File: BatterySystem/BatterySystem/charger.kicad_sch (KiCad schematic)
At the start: 0 parts

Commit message: BQ25895 toegevoegd in test pcb
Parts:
- added U2: BQ25895RTW, Package_DFN_QFN:Texas_S-PWQFN-N24_EP2.7x2.7mm_ThermalVias, symbol Battery_Management:BQ25895RTW
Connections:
- new net: U2.13 (BAT), U2.14 (BAT)
- new net: U2.15 (SYS), U2.16 (SYS)
- new net: U2.17 (PGND), U2.18 (PGND), U2.25 (PGND)
- new net: U2.19 (SW), U2.20 (SW)
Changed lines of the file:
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@@
 (kicad_sch (version 20230121) (generator eeschema)
   (paper "A4")
+  (symbol (lib_id "Battery_Management:BQ25895RTW") (at 119.38 93.98 0) (unit 1)
+    (in_bom yes) (on_board yes) (dnp no) (fields_autoplaced)
+    (property "Reference" "U2" (at 119.38 70.6501 0)
+      (effects (font (size 1.27 1.27)))
+    )
+    (property "Value" "BQ25895RTW" (at 119.38 72.5711 0)
+      (effects (font (size 1.27 1.27)))
+    )
+    (property "Footprint" "Package_DFN_QFN:Texas_S-PWQFN-N24_EP2.7x2.7mm_ThermalVias" (at 116.84 68.58 0)
+      (effects (font (size 1.27 1.27)) hide)
+    )
+    (property "Datasheet" "http://www.ti.com/lit/ds/symlink/bq25895.pdf" (at 114.3 73.66 0)
+      (effects (font (size 1.27 1.27)) hide)
+    )
+    (pin "1")
+    (pin "10")
+    (pin "11")
+    (pin "12")
+    (pin "13")
+    (pin "14")
+    (pin "15")
+    (pin "16")
+    (pin "17")
+    (pin "18")
+    (pin "19")
+    (pin "2")
+    (pin "20")
+    (pin "21")
+    (pin "22")
+    (pin "23")
+    (pin "24")
+    (pin "25")
+    (pin "3")
+    (pin "4")
+    (pin "5")
+    (pin "6")
+    (pin "7")
+    (pin "8")
+    (pin "9")
+    (instances
+      (project "BatterySystem"
+        (path "/087df5f5-f8bd-4aad-837d-9ee553cf1b81/c2cf6bc5-c7a7-4536-bd5f-b8479578647d"
+          (reference "U2") (unit 1)
+        )
+      )
+    )
+  )
 )

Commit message: Charger circuit gemaakt
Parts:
- added C10: 47n, symbol Device:C
- added C11, C12, C8: 10u, symbol Device:C
- added C6: 8.2u, symbol Device:C
- added C7: 1u, symbol Device:C
- added C9: 4.7u, symbol Device:C
- added D1: LED, symbol Device:LED
- added L2: 2.2u, symbol Device:L
- added R1: 260, symbol Device:R
- added R2: 5.23k, symbol Device:R
- added R3: 30.1k, symbol Device:R
- added R4: 2.2k, symbol Device:R
- added R5: 4.7k, symbol Device:R
- added R6, R7, R8: 10k, symbol Device:R
- added TH1: Thermistor, symbol Device:Thermistor
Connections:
- net Input: now reaches U2.1 (VBUS)
- net Input: now also C7.1
- net at U2.10 (ILIM): now also R1.2
- net at U2.11 (TS): now also R2.1, R3.2, TH1.1
- net Bat: now reaches U2.13 (BAT), U2.14 (BAT)
- net Bat: now also C8.2
- net 3.5-4.5V: now reaches U2.15 (SYS), U2.16 (SYS)
- net 3.5-4.5V: now also C11.2, C12.2, D1.2 (A), L2.2
- net GND: now reaches U2.17 (PGND), U2.18 (PGND), U2.25 (PGND)
- net GND: now also C11.1, C12.1, C6.2, C7.2, C8.1, C9.1, R1.1, R3.1, R5.1, TH1.2
- net at U2.19 (SW), U2.20 (SW): now also C10.2, L2.1
- net D+: now reaches U2.2 (D+)
- net at U2.21 (BTST): now also C10.1
- net at U2.22 (REGN): now also C9.2, R2.2
- net Phone: now reaches U2.23 (PMID)
- net Phone: now also C6.1
- net D-: now reaches U2.3 (D-)
- net at U2.4 (STAT): now also R4.2
- net at U2.5 (SCL): now also R7.2
- net at U2.6 (SDA): now also R6.2
- net at U2.7 (INT): now also R8.2
- net at U2.9 (~{CE}): now also R5.2
- new net: D1.1 (K), R4.1
- new net Vref: R6.1, R7.1, R8.1
- no-connect marks 0 -> 3

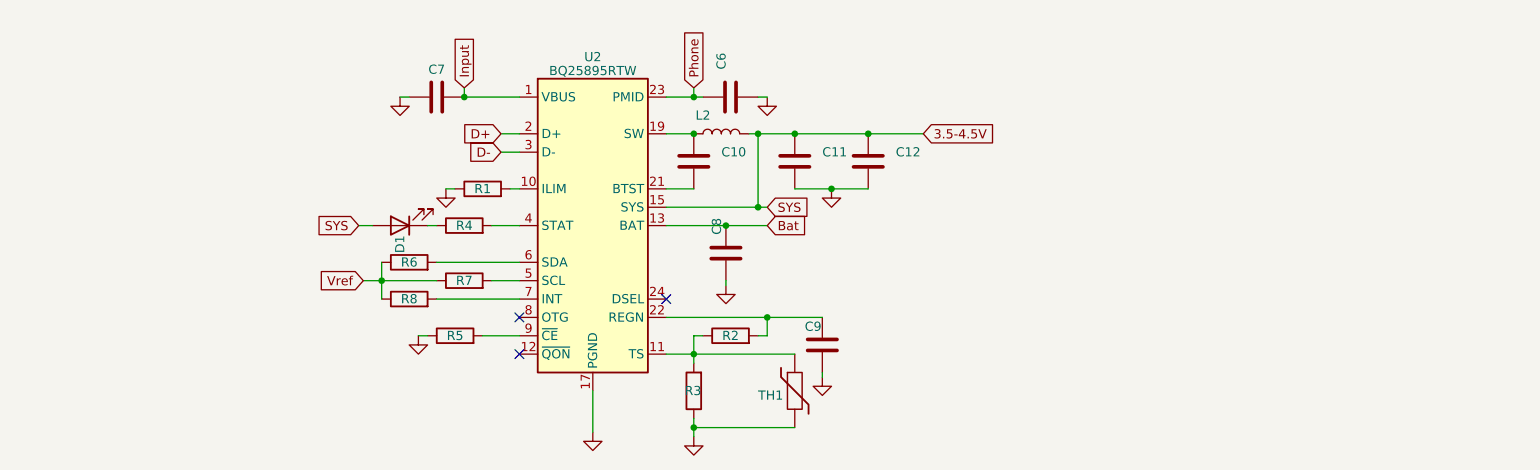
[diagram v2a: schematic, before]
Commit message: USB toegevoegd
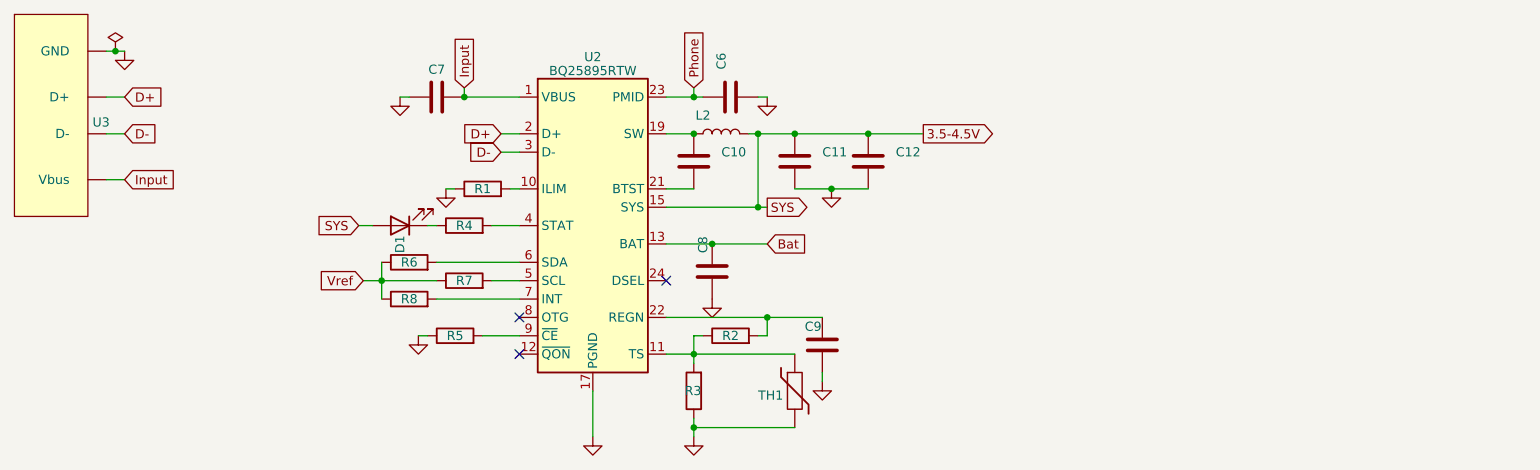
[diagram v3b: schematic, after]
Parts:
- added U3: ~, symbol usbc:USBC-THT
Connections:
- net D+: now also U3. (Vbus)
- net D-: now also U3. (Vbus)
- net GND: now also U3. (Vbus)
- net Input: now also U3. (Vbus)
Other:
- moved on the sheet: C8

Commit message: Footprints toegevoegd aan battery charger
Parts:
- removed U3: ~, symbol usbc:USBC-THT
- C10, C11, C12, C8, C9: footprint (none) -> Capacitor_SMD:C_0603_1608Metric
- C6: footprint (none) -> Capacitor_SMD:C_1206_3216Metric
- C7, R1, R2, R3, R4, R5, R6, R7, R8: footprint (none) -> Resistor_SMD:R_0603_1608Metric
- D1: footprint (none) -> LED_SMD:LED_0603_1608Metric
- TH1: value Thermistor -> 10k; footprint (none) -> Resistor_SMD:R_0603_1608Metric
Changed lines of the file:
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@@
   (junction (at 142.24 91.44) (diameter 0) (color 0 0 0 0)
-  )
-  (junction (at 53.34 69.85) (diameter 0) (color 0 0 0 0)
   )
   (junction (at 133.35 121.92) (diameter 0) (color 0 0 0 0)
@@
   (no_connect (at 129.54 101.6))
   (no_connect (at 109.22 111.76))
-  (wire (pts (xy 52.07 76.2) (xy 54.61 76.2))
-    (stroke (width 0) (type default))
-  )
   (wire (pts (xy 105.41 101.6) (xy 109.22 101.6))
     (stroke (width 0) (type default))
@@
     (stroke (width 0) (type default))
   )
-  (wire (pts (xy 52.07 81.28) (xy 54.61 81.28))
-    (stroke (width 0) (type default))
-  )
   (wire (pts (xy 105.41 93.98) (xy 109.22 93.98))
     (stroke (width 0) (type default))
@@
     (stroke (width 0) (type default))
   )
-  (wire (pts (xy 53.34 69.85) (xy 54.61 69.85))
-    (stroke (width 0) (type default))
-  )
   (wire (pts (xy 97.79 99.06) (xy 109.22 99.06))
     (stroke (width 0) (type default))
@@
     (stroke (width 0) (type default))
   )
-  (wire (pts (xy 52.07 87.63) (xy 54.61 87.63))
-    (stroke (width 0) (type default))
-  )
   (wire (pts (xy 129.54 111.76) (xy 133.35 111.76))
     (stroke (width 0) (type default))
@@
   )
   (wire (pts (xy 95.25 109.22) (xy 96.52 109.22))
-    (stroke (width 0) (type default))
-  )
-  (wire (pts (xy 52.07 69.85) (xy 53.34 69.85))
     (stroke (width 0) (type default))
   )
@@
     )
   )
-  (global_label "D+" (shape input) (at 54.61 76.2 0) (fields_autoplaced)
-    (effects (font (size 1.27 1.27)) (justify left))
-    (property "Intersheetrefs" "${INTERSHEET_REFS}" (at 60.3582 76.2 0)
-      (effects (font (size 1.27 1.27)) (justify left) hide)
-    )
-  )
   (global_label "SYS" (shape output) (at 143.51 91.44 0) (fields_autoplaced)
     (effects (font (size 1.27 1.27)) (justify left))
@@
     )
   )
-  (global_label "D-" (shape input) (at 54.61 81.28 0) (fields_autoplaced)
-    (effects (font (size 1.27 1.27)) (justify left))
-    (property "Intersheetrefs" "${INTERSHEET_REFS}" (at 60.3582 81.28 0)
-      (effects (font (size 1.27 1.27)) (justify left) hide)
-    )
-  )
   (global_label "D-" (shape input) (at 106.68 83.82 180) (fields_autoplaced)
     (effects (font (size 1.27 1.27)) (justify right))
@@
     )
   )
-  (global_label "Input" (shape input) (at 54.61 87.63 0) (fields_autoplaced)
-    (effects (font (size 1.27 1.27)) (justify left))
-    (property "Intersheetrefs" "${INTERSHEET_REFS}" (at 62.2933 87.63 0)
-      (effects (font (size 1.27 1.27)) (justify left) hide)
-    )
-  )
   (global_label "Phone" (shape input) (at 133.35 74.93 90) (fields_autoplaced)
     (effects (font (size 1.27 1.27)) (justify left))
@@
       (effects (font (size 1.27 1.27)) hide)
     )
-    (property "Footprint" "" (at 101.6 103.378 90)
+    (property "Footprint" "Resistor_SMD:R_0603_1608Metric" (at 101.6 103.378 90)
       (effects (font (size 1.27 1.27)) hide)
     )
@@
       (effects (font (size 1.27 1.27)) (justify left) hide)
     )
-    (property "Footprint" "" (at 142.24 75.2348 0)
+    (property "Footprint" "Capacitor_SMD:C_1206_3216Metric" (at 142.24 75.2348 0)
       (effects (font (size 1.27 1.27)) hide)
     )
@@
         (path "/087df5f5-f8bd-4aad-837d-9ee553cf1b81/c2cf6bc5-c7a7-4536-bd5f-b8479578647d"
           (reference "C6") (unit 1)
-        )
-      )
-    )
-  )
-  (symbol (lib_id "usbc:USBC-THT") (at 40.64 73.66 0) (unit 1)
-    (in_bom yes) (on_board yes) (dnp no) (fields_autoplaced)
-    (property "Reference" "U3" (at 50.165 79.6918 0)
-      (effects (font (size 1.27 1.27)) (justify left))
-    )
-    (property "Value" "~" (at 40.64 73.66 0)
-      (effects (font (size 1.27 1.27)))
-    )
-    (property "Footprint" "" (at 40.64 73.66 0)
-      (effects (font (size 1.27 1.27)) hide)
-    )
-    (property "Datasheet" "" (at 40.64 73.66 0)
-      (effects (font (size 1.27 1.27)) hide)
-    )
-    (pin "")
-    (pin "")
-    (pin "")
-    (pin "")
-    (instances
-      (project "BatterySystem"
-        (path "/087df5f5-f8bd-4aad-837d-9ee553cf1b81/c2cf6bc5-c7a7-4536-bd5f-b8479578647d"
-          (reference "U3") (unit 1)
         )
       )
@@
       (effects (font (size 1.27 1.27)) (justify right) hide)
     )
-    (property "Footprint" "" (at 135.128 116.84 90)
+    (property "Footprint" "Resistor_SMD:R_0603_1608Metric" (at 135.128 116.84 90)
       (effects (font (size 1.27 1.27)) hide)
     )
@@
       (effects (font (size 1.27 1.27)) (justify left))
     )
-    (property "Value" "Thermistor" (at 151.13 118.11 0)
+    (property "Value" "10k" (at 151.13 118.11 0)
       (effects (font (size 1.27 1.27)) (justify left) hide)
     )
-    (property "Footprint" "" (at 147.32 116.84 0)
+    (property "Footprint" "Resistor_SMD:R_0603_1608Metric" (at 147.32 116.84 0)
       (effects (font (size 1.27 1.27)) hide)
     )
@@
       (effects (font (size 1.27 1.27)) hide)
     )
-    (property "Footprint" "" (at 150.1648 106.68 0)
+    (property "Footprint" "Capacitor_SMD:C_0603_1608Metric" (at 150.1648 106.68 0)
       (effects (font (size 1.27 1.27)) hide)
     )
@@
     )
   )
-  (symbol (lib_id "power:GND") (at 54.61 69.85 0) (unit 1)
-    (in_bom yes) (on_board yes) (dnp no) (fields_autoplaced)
-    (property "Reference" "#PWR011" (at 54.61 76.2 0)
-      (effects (font (size 1.27 1.27)) hide)
-    )
-    (property "Value" "GND" (at 54.61 73.9855 0)
-      (effects (font (size 1.27 1.27)) hide)
-    )
-    (property "Footprint" "" (at 54.61 69.85 0)
-      (effects (font (size 1.27 1.27)) hide)
-    )
-    (property "Datasheet" "" (at 54.61 69.85 0)
-      (effects (font (size 1.27 1.27)) hide)
-    )
-    (pin "1")
-    (instances
-      (project "BatterySystem"
-        (path "/087df5f5-f8bd-4aad-837d-9ee553cf1b81/c2cf6bc5-c7a7-4536-bd5f-b8479578647d"
-          (reference "#PWR011") (unit 1)
-        )
-      )
-    )
-  )
   (symbol (lib_id "Device:R") (at 138.43 109.22 90) (unit 1)
     (in_bom yes) (on_board yes) (dnp no)
@@
       (effects (font (size 1.27 1.27)) hide)
     )
-    (property "Footprint" "" (at 138.43 110.998 90)
+    (property "Footprint" "Resistor_SMD:R_0603_1608Metric" (at 138.43 110.998 90)
       (effects (font (size 1.27 1.27)) hide)
     )
@@
       (effects (font (size 1.27 1.27)) hide)
     )
-    (property "Footprint" "" (at 93.98 105.918 90)
+    (property "Footprint" "Resistor_SMD:R_0603_1608Metric" (at 93.98 105.918 90)
       (effects (font (size 1.27 1.27)) hide)
     )
@@
       (effects (font (size 1.27 1.27)) hide)
     )
-    (property "Footprint" "" (at 100.33 110.998 90)
+    (property "Footprint" "Resistor_SMD:R_0603_1608Metric" (at 100.33 110.998 90)
       (effects (font (size 1.27 1.27)) hide)
     )
@@
         (path "/087df5f5-f8bd-4aad-837d-9ee553cf1b81/c2cf6bc5-c7a7-4536-bd5f-b8479578647d"
           (reference "#PWR08") (unit 1)
-        )
-      )
-    )
-  )
-  (symbol (lib_id "power:PWR_FLAG") (at 53.34 69.85 0) (unit 1)
-    (in_bom yes) (on_board yes) (dnp no) (fields_autoplaced)
-    (property "Reference" "#FLG01" (at 53.34 67.945 0)
-      (effects (font (size 1.27 1.27)) hide)
-    )
-    (property "Value" "PWR_FLAG" (at 53.34 66.3481 0)
-      (effects (font (size 1.27 1.27)) hide)
-    )
-    (property "Footprint" "" (at 53.34 69.85 0)
-      (effects (font (size 1.27 1.27)) hide)
-    )
-    (property "Datasheet" "~" (at 53.34 69.85 0)
-      (effects (font (size 1.27 1.27)) hide)
-    )
-    (pin "1")
-    (instances
-      (project "BatterySystem"
-        (path "/087df5f5-f8bd-4aad-837d-9ee553cf1b81/c2cf6bc5-c7a7-4536-bd5f-b8479578647d"
-          (reference "#FLG01") (unit 1)
         )
       )
@@
       (effects (font (size 1.27 1.27)) (justify right) hide)
     )
-    (property "Footprint" "" (at 92.71 93.98 0)
+    (property "Footprint" "LED_SMD:LED_0603_1608Metric" (at 92.71 93.98 0)
       (effects (font (size 1.27 1.27)) hide)
     )
@@
       (effects (font (size 1.27 1.27)) (justify right) hide)
     )
-    (property "Footprint" "" (at 156.5148 81.28 0)
+    (property "Footprint" "Capacitor_SMD:C_0603_1608Metric" (at 156.5148 81.28 0)
       (effects (font (size 1.27 1.27)) hide)
     )
@@
       (effects (font (size 1.27 1.27)) hide)
     )
-    (property "Footprint" "" (at 104.14 90.678 90)
+    (property "Footprint" "Resistor_SMD:R_0603_1608Metric" (at 104.14 90.678 90)
       (effects (font (size 1.27 1.27)) hide)
     )
@@
       (effects (font (size 1.27 1.27)) (justify right) hide)
     )
-    (property "Footprint" "" (at 134.9248 96.52 0)
+    (property "Footprint" "Capacitor_SMD:C_0603_1608Metric" (at 134.9248 96.52 0)
       (effects (font (size 1.27 1.27)) hide)
     )
@@
       (effects (font (size 1.27 1.27)) hide)
     )
-    (property "Footprint" "" (at 93.98 77.1652 0)
+    (property "Footprint" "Resistor_SMD:R_0603_1608Metric" (at 93.98 77.1652 0)
       (effects (font (size 1.27 1.27)) hide)
     )
@@
       (effects (font (size 1.27 1.27)) hide)
     )
-    (property "Footprint" "" (at 93.98 100.838 90)
+    (property "Footprint" "Resistor_SMD:R_0603_1608Metric" (at 93.98 100.838 90)
       (effects (font (size 1.27 1.27)) hide)
     )
@@
       (effects (font (size 1.27 1.27)) (justify right) hide)
     )
-    (property "Footprint" "" (at 132.3848 81.28 0)
+    (property "Footprint" "Capacitor_SMD:C_0603_1608Metric" (at 132.3848 81.28 0)
       (effects (font (size 1.27 1.27)) hide)
     )
@@
       (effects (font (size 1.27 1.27)) hide)
     )
-    (property "Footprint" "" (at 101.6 95.758 90)
+    (property "Footprint" "Resistor_SMD:R_0603_1608Metric" (at 101.6 95.758 90)
       (effects (font (size 1.27 1.27)) hide)
     )
@@
       (effects (font (size 1.27 1.27)) (justify right) hide)
     )
-    (property "Footprint" "" (at 146.3548 81.28 0)
-      (effects (font (size 1.27 1.27)) hide)
-    )
+    (property "Footprint" "Capacitor_SMD:C_0603_1608Metric" (at 146.3548 81.28 0)
+      (effects (font (size 1.27 1.27)) hide)
+    )

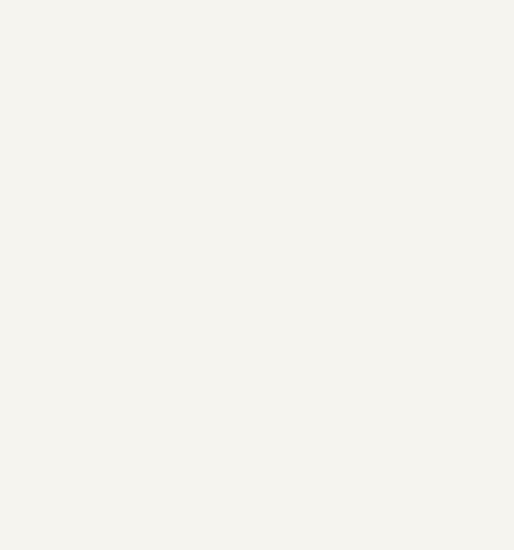
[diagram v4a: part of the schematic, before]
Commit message: Batterij en houder toegevoegd
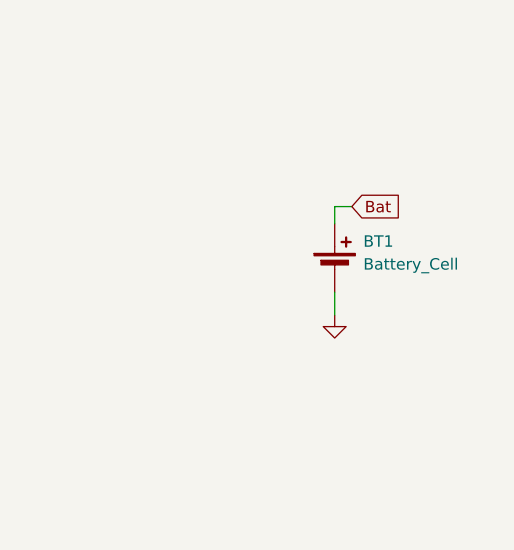
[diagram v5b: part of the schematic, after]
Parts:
- added BT1: Battery_Cell, Battery:BatteryHolder_Keystone_1042_1x18650, symbol Device:Battery_Cell
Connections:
- net Bat: now also BT1.1 (+)
- net GND: now also BT1.2 (-)
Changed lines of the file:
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@@
+    (stroke (width 0) (type default))
+  )
+  (wire (pts (xy 230.505 95.885) (xy 230.505 98.425))
     (stroke (width 0) (type default))
   )
@@
     (stroke (width 0) (type default))
   )
+  (wire (pts (xy 230.505 86.36) (xy 232.41 86.36))
+    (stroke (width 0) (type default))
+  )
   (wire (pts (xy 119.38 116.84) (xy 119.38 123.19))
     (stroke (width 0) (type default))
@@
   )
   (wire (pts (xy 106.68 81.28) (xy 109.22 81.28))
+    (stroke (width 0) (type default))
+  )
+  (wire (pts (xy 230.505 86.36) (xy 230.505 88.265))
     (stroke (width 0) (type default))
   )
@@
     (effects (font (size 1.27 1.27)) (justify left))
     (property "Intersheetrefs" "${INTERSHEET_REFS}" (at 176.7144 81.28 0)
+      (effects (font (size 1.27 1.27)) (justify left) hide)
+    )
+  )
+  (global_label "Bat" (shape input) (at 232.41 86.36 0) (fields_autoplaced)
+    (effects (font (size 1.27 1.27)) (justify left))
+    (property "Intersheetrefs" "${INTERSHEET_REFS}" (at 238.4605 86.36 0)
       (effects (font (size 1.27 1.27)) (justify left) hide)
     )
@@
     )
   )
+  (symbol (lib_id "Device:Battery_Cell") (at 230.505 93.345 0) (unit 1)
+    (in_bom yes) (on_board yes) (dnp no) (fields_autoplaced)
+    (property "Reference" "BT1" (at 233.68 90.2335 0)
+      (effects (font (size 1.27 1.27)) (justify left))
+    )
+    (property "Value" "Battery_Cell" (at 233.68 92.7735 0)
+      (effects (font (size 1.27 1.27)) (justify left))
+    )
+    (property "Footprint" "Battery:BatteryHolder_Keystone_1042_1x18650" (at 230.505 91.821 90)
+      (effects (font (size 1.27 1.27)) hide)
+    )
+    (property "Datasheet" "~" (at 230.505 91.821 90)
+      (effects (font (size 1.27 1.27)) hide)
+    )
+    (pin "1")
+    (pin "2")
+    (instances
+      (project "BatterySystem"
+        (path "/087df5f5-f8bd-4aad-837d-9ee553cf1b81/c2cf6bc5-c7a7-4536-bd5f-b8479578647d"
+          (reference "BT1") (unit 1)
+        )
+      )
+    )
+  )
   (symbol (lib_id "Device:R") (at 93.98 99.06 90) (unit 1)
     (in_bom yes) (on_board yes) (dnp no)
@@
         )
       )
+    )
+  )
+  (symbol (lib_id "power:GND") (at 230.505 98.425 0) (unit 1)
+    (in_bom yes) (on_board yes) (dnp no) (fields_autoplaced)
+    (property "Reference" "#PWR012" (at 230.505 104.775 0)
+      (effects (font (size 1.27 1.27)) hide)
+    )
+    (property "Value" "GND" (at 230.505 103.505 0)
+      (effects (font (size 1.27 1.27)) hide)
+    )
+    (property "Footprint" "" (at 230.505 98.425 0)
+      (effects (font (size 1.27 1.27)) hide)
+    )
+    (property "Datasheet" "" (at 230.505 98.425 0)
+      (effects (font (size 1.27 1.27)) hide)
+    )
+    (pin "1")
+    (instances
+      (project "BatterySystem"
+        (path "/087df5f5-f8bd-4aad-837d-9ee553cf1b81/c2cf6bc5-c7a7-4536-bd5f-b8479578647d"
+          (reference "#PWR012") (unit 1)
+        )
+      )
